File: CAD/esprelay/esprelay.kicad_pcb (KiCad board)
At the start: 2 copper layers, 65 x 20 mm, 54 parts, among them J1 Conn_01x06_Pin, J2 Conn_01x14_Pin, K1 G6K-2P-Y, K2 G6K-2P-Y, K3 G6K-2P-Y, Q1 Q_Photo_NPN, SW1 SW_SPST, U1 SPX3819M5-L-5-0, U2 SPX3819M5-L-3-3, U3 ESP-12F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

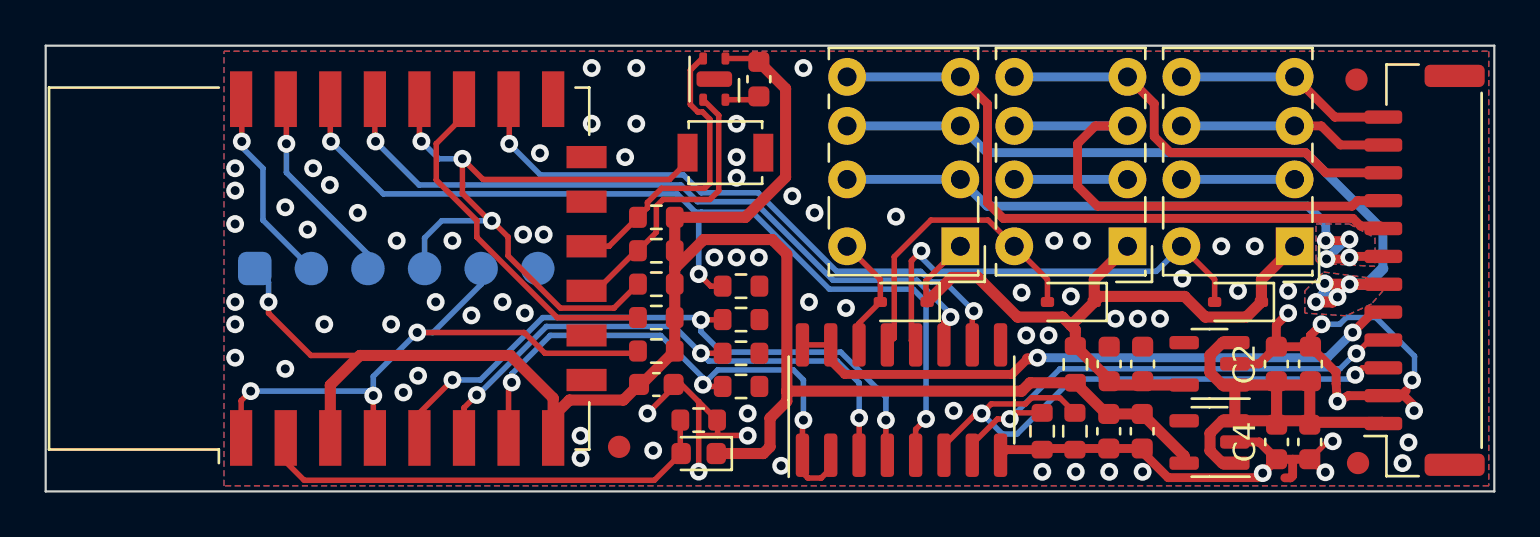
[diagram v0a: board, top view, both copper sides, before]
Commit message: Feat: JLC purchase
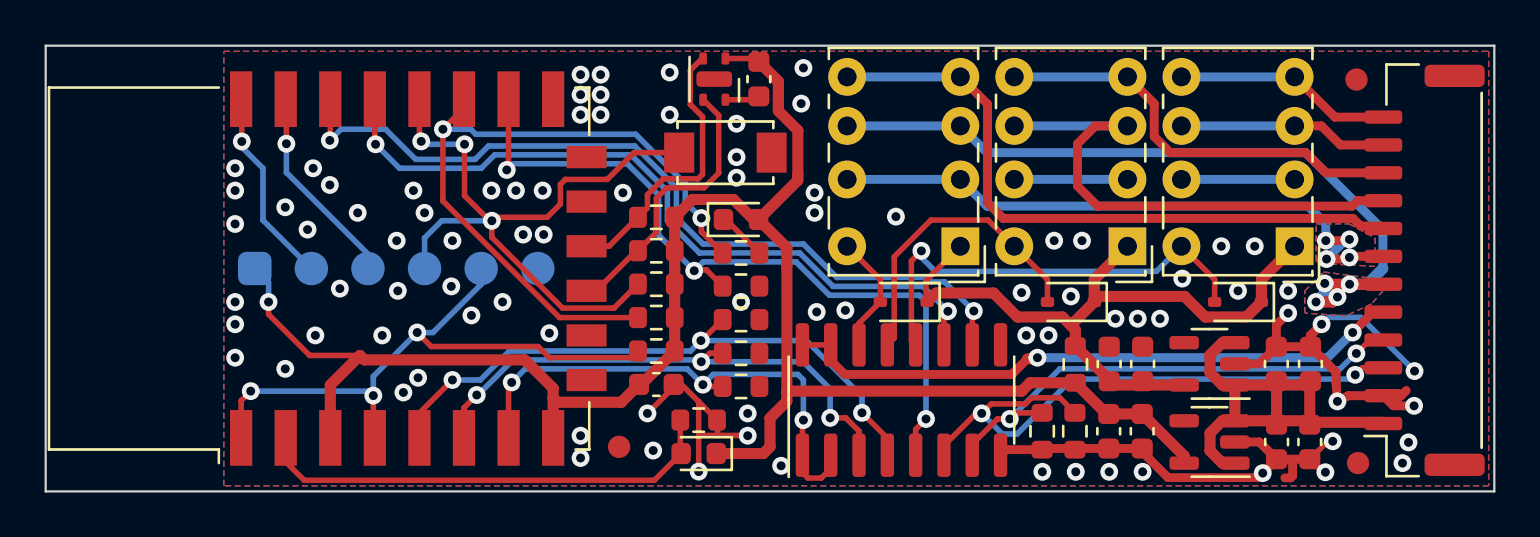
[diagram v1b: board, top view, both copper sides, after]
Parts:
- added D4: KT-0603R, LED_SMD:LED_0603_1608Metric, F.Cu at (131.2, 80.3)
- added R13: 470, Resistor_SMD:R_0603_1608Metric, F.Cu at (131.2, 81.8)
- SW1: footprint Button_Switch_SMD:SW_SPST_B3U-1000P -> Button_Switch_SMD:SW_SPST_TS-1088-AR
- U5: value ULN2003A -> TBD62003AFWG
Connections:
- net Net-(U3-GPIO2) renamed GPIO2
- R10 pad 1: GPIO5 -> GPIO15
- U5 pad 10: GPIO15 -> GPIO5
- U5 pad 5: GPIO5 -> GPIO15
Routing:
- net GPIO2: track 16.2 -> 31.6 mm, vias 0 -> 2
- net GPIO15: track 27.5 -> 34.8 mm, vias 2 -> 3
- net GPIO5: track 42.8 -> 37.2 mm, vias 3 -> 2
- net +3.3V: track 86.2 -> 83.2 mm
- net Net-(D4-K): track 0.00 -> 2.23 mm
- net GPIO13: track 25.5 -> 23.7 mm
- net GPIO12: track 25.9 -> 24.2 mm
- net GPIO14: track 29.2 -> 27.8 mm
- net GPIO4: track 32.5 -> 33.7 mm
- net GND: track 54.3 -> 53.2 mm, vias 79 -> 87
- net SCL: track 13.2 -> 12.6 mm
- net VBUS: track 33.6 -> 33.0 mm

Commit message: Feat: 4 layer,readme and cleanup
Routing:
- net GND: track 53.2 -> 54.1 mm, vias 87 -> 91
- net GPIO15: track 34.8 -> 33.9 mm
- net +3.3V: track 83.2 -> 82.7 mm
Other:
- outline, holes or cut-outs redrawn

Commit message: Simplification
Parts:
- removed C10: 0.1uF, Capacitor_SMD:C_0603_1608Metric
- removed D3: 1N4148WS, Diode_SMD:D_SOD-323
- removed D4: KT-0603R, LED_SMD:LED_0603_1608Metric
- removed FID1, FID2, FID3: Fiducial, Fiducial:Fiducial_1mm_Mask2mm
- removed JP1: Jumper_2_Open, Resistor_SMD:R_0603_1608Metric
- removed K3: G6K-2P-Y, Relay_THT:Relay_DPDT_Omron_G6K-2P-Y
- removed Q1: Q_Photo_NPN, LED_SMD:LED_0603_1608Metric
- removed R13: 470, Resistor_SMD:R_0603_1608Metric
- removed R4, R5: 10K, Resistor_SMD:R_0603_1608Metric
- removed SW1: SW_SPST, Button_Switch_SMD:SW_SPST_TS-1088-AR
- removed U4: SHTC3, Sensor_Humidity:Sensirion_DFN-4-1EP_2x2mm_P1mm_EP0.7x1.6mm
- removed kibuzzard-65666CB0: G***, kibuzzard-65666CB0
- removed kibuzzard-65666CF7: G***, kibuzzard-65666CF7
- removed kibuzzard-65666CFD: G***, kibuzzard-65666CFD
- removed kibuzzard-65666D06: G***, kibuzzard-65666D06
- removed kibuzzard-65666D10: G***, kibuzzard-65666D10
- removed kibuzzard-65666D19: G***, kibuzzard-65666D19
- added kibuzzard-65CFDA91: G***, kibuzzard-65CFDA91, B.Cu at (149.1, 83.3)
- added kibuzzard-65CFDAA0: G***, kibuzzard-65CFDAA0, B.Cu at (149.1, 80.2)
- added kibuzzard-65CFDAA7: G***, kibuzzard-65CFDAA7, B.Cu at (149.1, 78.7)
- added kibuzzard-65CFDAAD: G***, kibuzzard-65CFDAAD, B.Cu at (149.1, 77.1)
- added kibuzzard-65CFDAB5: G***, kibuzzard-65CFDAB5, B.Cu at (149.1, 75.6)
- added kibuzzard-65CFDABC: G***, kibuzzard-65CFDABC, B.Cu at (149.1, 74.0)
- C1, C2, C6, C7: value 22uF -> 2.2uF; footprint Capacitor_SMD:C_0603_1608Metric -> Capacitor_SMD:C_0402_1005Metric
- C3, C4, C5, C8, C9: footprint Capacitor_SMD:C_0603_1608Metric -> Capacitor_SMD:C_0402_1005Metric
- J2: value Conn_01x14_Pin -> SM12B-GHS-TB(LF)(SN)
- R1, R10, R11, R12, R2, R7, R8, R9: footprint Resistor_SMD:R_0603_1608Metric -> Resistor_SMD:R_0402_1005Metric
- R3: value 10K -> 137k; footprint Resistor_SMD:R_0603_1608Metric -> Resistor_SMD:R_0402_1005Metric
- R6: value 470 -> 316k; footprint Resistor_SMD:R_0603_1608Metric -> Resistor_SMD:R_0402_1005Metric
- U1: value SPX3819M5-L-5-0 -> DS8242-33S5
- U2: value SPX3819M5-L-3-3 -> DS8242-50S3
- moved R3 14.8 mm to (140.6, 91.3), turned to 180 degrees
- moved R6 14.0 mm to (143.1, 91.3), turned to 180 degrees
- moved kibuzzard-65666C7B 13.0 mm to (149.1, 86.4)
- moved kibuzzard-65666C6B 13.0 mm to (149.1, 91.1)
- moved kibuzzard-65666C71 13.0 mm to (149.1, 89.5)
- moved kibuzzard-65666C76 13.0 mm to (149.1, 88.0)
- moved kibuzzard-65666C87 13.0 mm to (149.1, 84.9)
- moved kibuzzard-65666CB7 13.0 mm to (149.1, 81.8)
- moved J2 12.9 mm to (149.0, 82.6)
- moved C5 12.5 mm to (144.3, 87.1), turned to 90 degrees
- moved U2 11.5 mm to (141.7, 85.5)
- moved C1 11.4 mm to (145.3, 89.9), turned to 90 degrees
- moved C8 11.3 mm to (137.9, 86.0), turned to -90 degrees
- moved C4 11.0 mm to (144.3, 89.9), turned to -90 degrees
- moved U1 10.7 mm to (141.7, 89.0)
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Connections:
- J2 pad 10: R2NO -> R2NC
- J2 pad 11: R3A -> R2CO
- J2 pad 12: R3NO -> R2NO
- J2 pad 6: R1A -> HO2
- J2 pad 8: R1NO -> R1CO
- J2 pad 9: R2A -> R1NO
- K1 pad 3: R1A -> R1CO
- K1 pad 6: R1A -> R1CO
- K2 pad 3: R2A -> R2CO
- K2 pad 6: R2A -> R2CO
- R3 pad 1: GPIO2 -> ADC
- R3 pad 2: +3.3V -> GND
- R6 pad 1: PHOTO_OUT -> +VDC
- R6 pad 2: GND -> ADC
- U1 pad 3: +VDC -> unconnected-(U1-NC-Pad3)
- U1 pad 5: VBUS -> +3.3V
- U2 pad 3: +VDC -> unconnected-(U2-NC-Pad3)
- U2 pad 5: +3.3V -> VBUS
- U3 pad 11: SDA -> unconnected-(U3-GPIO9-Pad11)
- U3 pad 12: SCL -> unconnected-(U3-GPIO10-Pad12)
- U3 pad 17: GPIO2 -> unconnected-(U3-GPIO2-Pad17)
- U3 pad 2: PHOTO_OUT -> ADC
- U5 pad 12: RO3 -> RO2
- U5 pad 13: RO2 -> RO1
- U5 pad 14: RO1 -> HO2
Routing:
- net GND: track 54.1 -> 12.3 mm, vias 91 -> 70
- net ADC: track 0.00 -> 35.3 mm, vias 0 -> 2
- net R1A: track 34.2 -> 0.00 mm, vias 4 -> 0
- net +3.3V: track 82.7 -> 48.8 mm, vias 1 -> 3
- net GPIO2: track 31.6 -> 0.00 mm, vias 2 -> 0
- net R2A: track 23.7 -> 0.00 mm
- net HO2: track 0.00 -> 21.7 mm, vias 0 -> 2
- net R1CO: track 0.00 -> 21.2 mm
- net PHOTO_OUT: track 21.2 -> 0.00 mm
- net RO3: track 20.3 -> 0.00 mm, vias 1 -> 0
- net VBUS: track 33.0 -> 17.4 mm
- net SDA: track 12.6 -> 0.00 mm
- net SCL: track 12.6 -> 0.00 mm
- net R2CO: track 0.00 -> 10.7 mm
- net BOOT: track 32.3 -> 22.0 mm
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- removed copper zone on B.Cu, net R1A
- removed copper zone on F.Cu, net R1A
- removed copper zone on B.Cu, net R1NC
- removed copper zone on F.Cu, net R1NC
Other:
- board size 65 x 20 mm -> 52.2 x 20 mm
